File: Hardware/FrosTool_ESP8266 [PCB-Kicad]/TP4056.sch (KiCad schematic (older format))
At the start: 9 parts

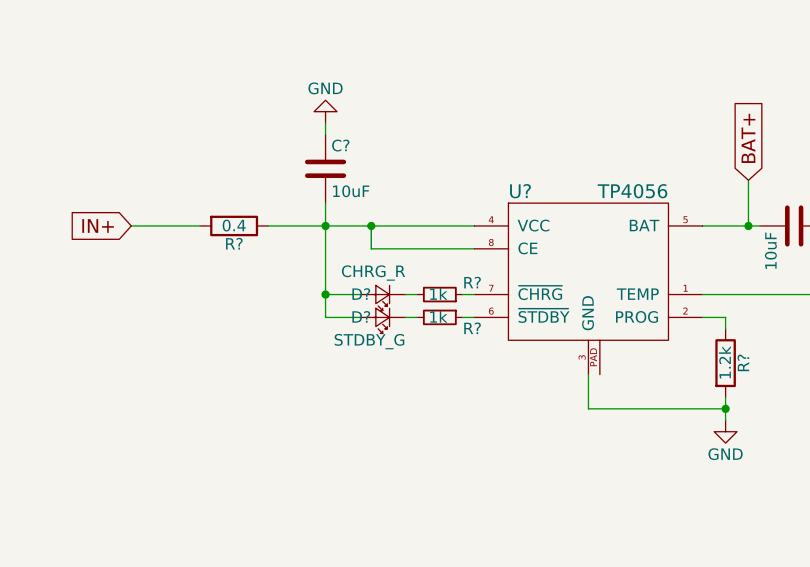
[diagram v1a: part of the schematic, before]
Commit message: Removed the old TP4056 component
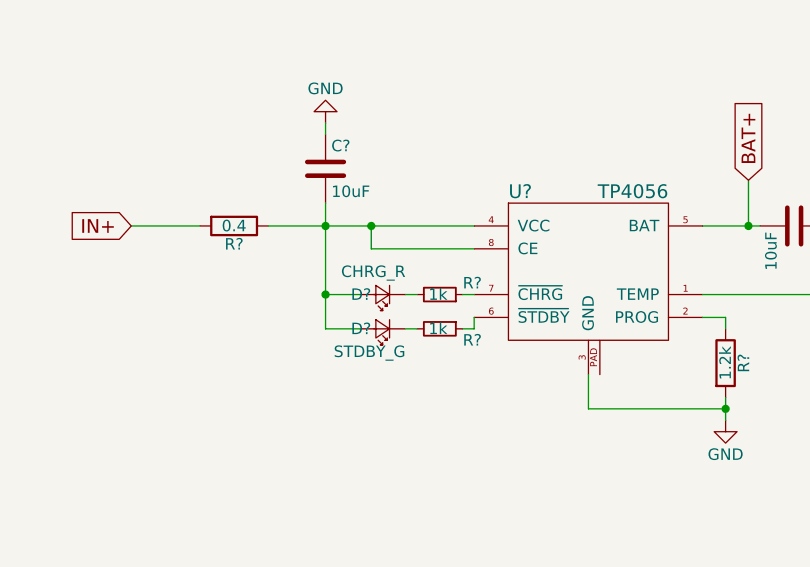
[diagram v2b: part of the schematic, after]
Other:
- moved on the sheet: D?, R?
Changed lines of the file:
@@
 L R_Small R?
 U 1 1 59DACB2A
-P 2500 2600
-F 0 "R?" V 2550 2700 50  0000 L CNN
-F 1 "1k" V 2500 2550 50  0000 L CNN
-F 2 "" H 2500 2600 50  0001 C CNN
-F 3 "" H 2500 2600 50  0001 C CNN
-	1    2500 2600
+P 2500 2650
+F 0 "R?" V 2550 2750 50  0000 L CNN
+F 1 "1k" V 2500 2600 50  0000 L CNN
+F 2 "" H 2500 2650 50  0001 C CNN
+F 3 "" H 2500 2650 50  0001 C CNN
+	1    2500 2650
 	0    1    1    0
 $EndComp
 Wire Wire Line
-	2600 2600 2650 2600
+	2600 2650 2650 2650
 $Comp
 L LED_Small D?
@@
 L LED_Small D?
 U 1 1 59DACFE4
-P 2250 2600
-F 0 "D?" H 2300 2600 50  0000 L CNN
-F 1 "STDBY_G" H 2150 2700 50  0000 L CNN
-F 2 "" V 2250 2600 50  0001 C CNN
-F 3 "" V 2250 2600 50  0001 C CNN
-	1    2250 2600
+P 2250 2650
+F 0 "D?" H 2300 2650 50  0000 L CNN
+F 1 "STDBY_G" H 2150 2750 50  0000 L CNN
+F 2 "" V 2250 2650 50  0001 C CNN
+F 3 "" V 2250 2650 50  0001 C CNN
+	1    2250 2650
 	-1   0    0    1
 $EndComp
 Wire Wire Line
-	2400 2600 2350 2600
+	2400 2650 2350 2650
 Wire Wire Line
-	2150 2500 2000 2500
+	2000 2500 2150 2500
 Wire Wire Line
-	2000 2100 2000 2600
-Connection ~ 2000 2200
-Wire Wire Line
-	2000 2600 2150 2600
+	2000 2650 2150 2650
 Connection ~ 2000 2500
 Wire Wire Line
@@
 Text Notes 650  1100 0    394  ~ 79
 TP4056
+Wire Wire Line
+	2000 2100 2000 2650
+Connection ~ 2000 2200
+Wire Wire Line
+	2650 2650 2650 2600
 $EndSCHEMATC

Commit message: Added NETList
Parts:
- gave numbers to parts that had none: 9
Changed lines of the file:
@@
 $EndDescr
 $Comp
-L TP4056 U?
+L TP4056 U3
 U 1 1 59DAA881
 P 3150 2450
-F 0 "U?" H 2800 2850 60  0000 L CNN
+F 0 "U3" H 2800 2850 60  0000 L CNN
 F 1 "TP4056" H 3500 2850 60  0000 R CNN
 F 2 "" H 3150 2450 60  0000 C CNN
@@
 IN+
 $Comp
-L R R?
+L R R6
 U 1 1 59DAAB4A
 P 1600 2200
-F 0 "R?" V 1680 2200 50  0000 C CNN
+F 0 "R6" V 1680 2200 50  0000 C CNN
 F 1 "0.4" V 1600 2200 50  0000 C CNN
 F 2 "" V 1530 2200 50  0001 C CNN
@@
 	3150 2850 3150 3000
 $Comp
-L GND #PWR?
+L GND #PWR18
 U 1 1 59DAB02E
 P 2000 1750
-F 0 "#PWR?" H 2000 1500 50  0001 C CNN
+F 0 "#PWR18" H 2000 1500 50  0001 C CNN
 F 1 "GND" H 2000 1600 50  0000 C CNN
 F 2 "" H 2000 1750 50  0001 C CNN
@@
 	3650 2500 4250 2500
 $Comp
-L C C?
+L C C3
 U 1 1 59DAB50D
 P 2000 1950
-F 0 "C?" H 2025 2050 50  0000 L CNN
+F 0 "C3" H 2025 2050 50  0000 L CNN
 F 1 "10uF" H 2025 1850 50  0000 L CNN
 F 2 "" H 2038 1800 50  0001 C CNN
@@
 TODO
 $Comp
-L R R?
+L R R9
 U 1 1 59DABBF0
 P 3750 2800
-F 0 "R?" V 3830 2800 50  0000 C CNN
+F 0 "R9" V 3830 2800 50  0000 C CNN
 F 1 "1.2k" V 3750 2800 50  0000 C CNN
 F 2 "" V 3680 2800 50  0001 C CNN
@@
 $EndComp
 $Comp
-L GND #PWR?
+L GND #PWR19
 U 1 1 59DABC8B
 P 3750 3050
-F 0 "#PWR?" H 3750 2800 50  0001 C CNN
+F 0 "#PWR19" H 3750 2800 50  0001 C CNN
 F 1 "GND" H 3750 2900 50  0000 C CNN
 F 2 "" H 3750 3050 50  0001 C CNN
@@
 	3650 2200 3900 2200
 $Comp
-L C C?
+L C C4
 U 1 1 59DAC301
 P 4050 2200
-F 0 "C?" H 4075 2300 50  0000 L CNN
+F 0 "C4" H 4075 2300 50  0000 L CNN
 F 1 "10uF" H 4075 2100 50  0000 L CNN
 F 2 "" H 4088 2050 50  0001 C CNN
@@
 	4250 2500 4250 2200
 $Comp
-L GND #PWR?
+L GND #PWR20
 U 1 1 59DAC4CB
 P 4350 2200
-F 0 "#PWR?" H 4350 1950 50  0001 C CNN
+F 0 "#PWR20" H 4350 1950 50  0001 C CNN
 F 1 "GND" H 4350 2050 50  0000 C CNN
 F 2 "" H 4350 2200 50  0001 C CNN
@@
 Connection ~ 3750 3000
 $Comp
-L R_Small R?
+L R_Small R7
 U 1 1 59DAC9F8
 P 2500 2500
-F 0 "R?" V 2550 2600 50  0000 L CNN
+F 0 "R7" V 2550 2600 50  0000 L CNN
 F 1 "1k" V 2500 2450 50  0000 L CNN
 F 2 "" H 2500 2500 50  0001 C CNN
@@
 	2650 2500 2600 2500
 $Comp
-L R_Small R?
+L R_Small R8
 U 1 1 59DACB2A
 P 2500 2650
-F 0 "R?" V 2550 2750 50  0000 L CNN
+F 0 "R8" V 2550 2750 50  0000 L CNN
 F 1 "1k" V 2500 2600 50  0000 L CNN
 F 2 "" H 2500 2650 50  0001 C CNN
@@
 	2600 2650 2650 2650
 $Comp
-L LED_Small D?
+L LED_Small D2
 U 1 1 59DACCBF
 P 2250 2500
-F 0 "D?" H 2300 2500 50  0000 L CNN
+F 0 "D2" H 2300 2500 50  0000 L CNN
 F 1 "CHRG_R" H 2150 2400 50  0000 L CNN
 F 2 "" V 2250 2500 50  0001 C CNN
@@
 	2400 2500 2350 2500
 $Comp
-L LED_Small D?
+L LED_Small D3
 U 1 1 59DACFE4
 P 2250 2650
-F 0 "D?" H 2300 2650 50  0000 L CNN
+F 0 "D3" H 2300 2650 50  0000 L CNN
 F 1 "STDBY_G" H 2150 2750 50  0000 L CNN
 F 2 "" V 2250 2650 50  0001 C CNN

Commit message: Footprints
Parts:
- C3: footprint (none) -> Capacitors_SMD:c_elec_3x5.3
- C4: footprint (none) -> Capacitors_SMD:C_0805
- D2, D3: footprint (none) -> LEDs:LED-3MM
- R6, R7, R8, R9: footprint (none) -> Resistors_SMD:R_1206
- U3: footprint (none) -> Housings_SOIC:SOIC-8_3.9x4.9mm_Pitch1.27mm
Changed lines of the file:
@@
 F 0 "U3" H 2800 2850 60  0000 L CNN
 F 1 "TP4056" H 3500 2850 60  0000 R CNN
-F 2 "" H 3150 2450 60  0000 C CNN
+F 2 "Housings_SOIC:SOIC-8_3.9x4.9mm_Pitch1.27mm" H 3150 2450 60  0001 C CNN
 F 3 "" H 3150 2450 60  0000 C CNN
 	1    3150 2450
@@
 F 0 "R6" V 1680 2200 50  0000 C CNN
 F 1 "0.4" V 1600 2200 50  0000 C CNN
-F 2 "" V 1530 2200 50  0001 C CNN
+F 2 "Resistors_SMD:R_1206" V 1530 2200 50  0001 C CNN
 F 3 "" H 1600 2200 50  0001 C CNN
 	1    1600 2200
@@
 	3150 2850 3150 3000
 $Comp
-L GND #PWR18
+L GND #PWR018
 U 1 1 59DAB02E
 P 2000 1750
-F 0 "#PWR18" H 2000 1500 50  0001 C CNN
+F 0 "#PWR018" H 2000 1500 50  0001 C CNN
 F 1 "GND" H 2000 1600 50  0000 C CNN
 F 2 "" H 2000 1750 50  0001 C CNN
@@
 F 0 "C3" H 2025 2050 50  0000 L CNN
 F 1 "10uF" H 2025 1850 50  0000 L CNN
-F 2 "" H 2038 1800 50  0001 C CNN
+F 2 "Capacitors_SMD:c_elec_3x5.3" H 2038 1800 50  0001 C CNN
 F 3 "" H 2000 1950 50  0001 C CNN
 	1    2000 1950
@@
 F 0 "R9" V 3830 2800 50  0000 C CNN
 F 1 "1.2k" V 3750 2800 50  0000 C CNN
-F 2 "" V 3680 2800 50  0001 C CNN
+F 2 "Resistors_SMD:R_1206" V 3680 2800 50  0001 C CNN
 F 3 "" H 3750 2800 50  0001 C CNN
 	1    3750 2800
@@
 $EndComp
 $Comp
-L GND #PWR19
+L GND #PWR019
 U 1 1 59DABC8B
 P 3750 3050
-F 0 "#PWR19" H 3750 2800 50  0001 C CNN
+F 0 "#PWR019" H 3750 2800 50  0001 C CNN
 F 1 "GND" H 3750 2900 50  0000 C CNN
 F 2 "" H 3750 3050 50  0001 C CNN
@@
 F 0 "C4" H 4075 2300 50  0000 L CNN
 F 1 "10uF" H 4075 2100 50  0000 L CNN
-F 2 "" H 4088 2050 50  0001 C CNN
+F 2 "Capacitors_SMD:C_0805" H 4088 2050 50  0001 C CNN
 F 3 "" H 4050 2200 50  0001 C CNN
 	1    4050 2200
@@
 	4250 2500 4250 2200
 $Comp
-L GND #PWR20
+L GND #PWR020
 U 1 1 59DAC4CB
 P 4350 2200
-F 0 "#PWR20" H 4350 1950 50  0001 C CNN
+F 0 "#PWR020" H 4350 1950 50  0001 C CNN
 F 1 "GND" H 4350 2050 50  0000 C CNN
 F 2 "" H 4350 2200 50  0001 C CNN
@@
 F 0 "R7" V 2550 2600 50  0000 L CNN
 F 1 "1k" V 2500 2450 50  0000 L CNN
-F 2 "" H 2500 2500 50  0001 C CNN
+F 2 "Resistors_SMD:R_1206" H 2500 2500 50  0001 C CNN
 F 3 "" H 2500 2500 50  0001 C CNN
 	1    2500 2500
@@
 F 0 "R8" V 2550 2750 50  0000 L CNN
 F 1 "1k" V 2500 2600 50  0000 L CNN
-F 2 "" H 2500 2650 50  0001 C CNN
+F 2 "Resistors_SMD:R_1206" H 2500 2650 50  0001 C CNN
 F 3 "" H 2500 2650 50  0001 C CNN
 	1    2500 2650
@@
 F 0 "D2" H 2300 2500 50  0000 L CNN
 F 1 "CHRG_R" H 2150 2400 50  0000 L CNN
-F 2 "" V 2250 2500 50  0001 C CNN
+F 2 "LEDs:LED-3MM" V 2250 2500 50  0001 C CNN
 F 3 "" V 2250 2500 50  0001 C CNN
 	1    2250 2500
@@
 F 0 "D3" H 2300 2650 50  0000 L CNN
 F 1 "STDBY_G" H 2150 2750 50  0000 L CNN
-F 2 "" V 2250 2650 50  0001 C CNN
+F 2 "LEDs:LED-3MM" V 2250 2650 50  0001 C CNN
 F 3 "" V 2250 2650 50  0001 C CNN
 	1    2250 2650

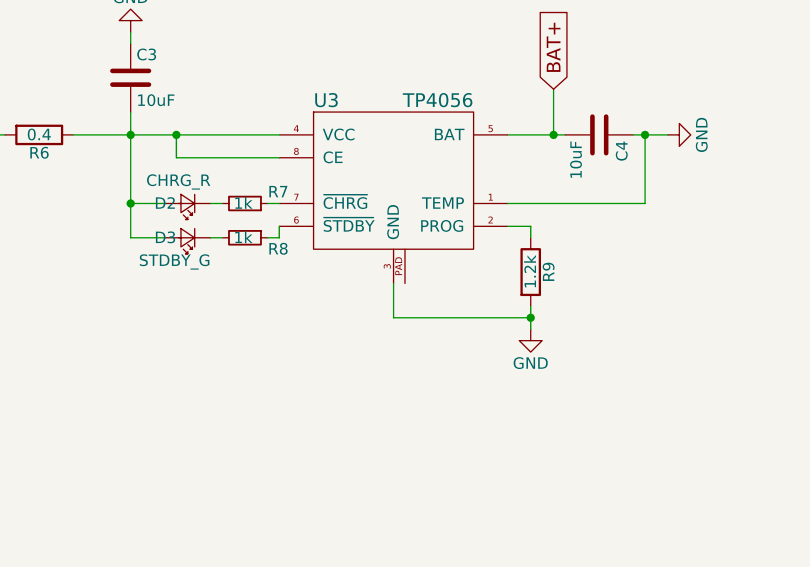
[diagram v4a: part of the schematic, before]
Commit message: Tracks and Vias improvement Bug Fixed: Pads Regulator
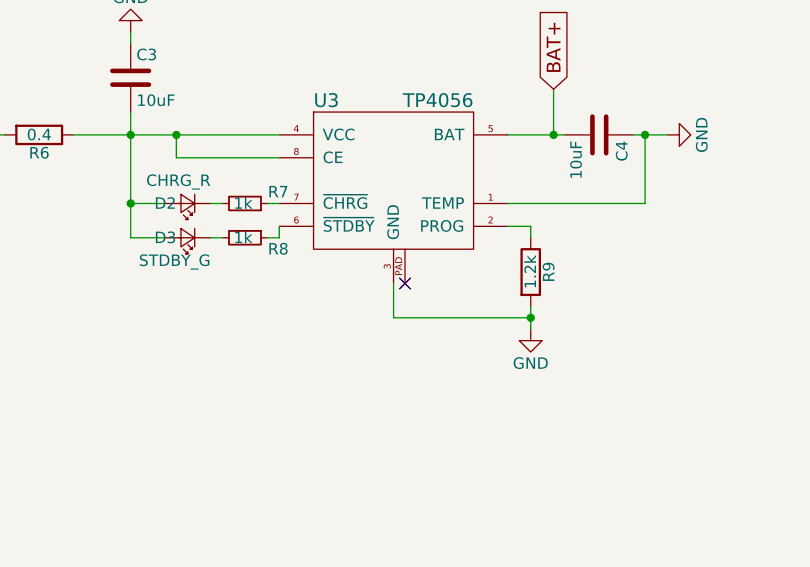
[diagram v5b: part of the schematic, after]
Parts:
- C3: footprint Capacitors_SMD:c_elec_3x5.3 -> Capacitors_SMD:c_elec_4x5.3
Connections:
- no-connect marks 0 -> 1
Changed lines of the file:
@@
 LIBS:tp4056
 LIBS:switches
+LIBS:ht7333-1
 LIBS:FrosTool_ESP8266-cache
 EELAYER 25 0
@@
 F 0 "C3" H 2025 2050 50  0000 L CNN
 F 1 "10uF" H 2025 1850 50  0000 L CNN
-F 2 "Capacitors_SMD:c_elec_3x5.3" H 2038 1800 50  0001 C CNN
+F 2 "Capacitors_SMD:c_elec_4x5.3" H 2038 1800 50  0001 C CNN
 F 3 "" H 2000 1950 50  0001 C CNN
 	1    2000 1950
@@
 Wire Wire Line
 	2650 2650 2650 2600
+NoConn ~ 3200 2850
 $EndSCHEMATC
